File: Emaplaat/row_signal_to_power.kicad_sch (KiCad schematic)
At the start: 11 parts, among them IC2 1EDN7550BXTSA1, IC4 74HC1G04GV-Q100H, IC5 1EDN7550BXTSA1, IC6 74LVC1G66GW,125

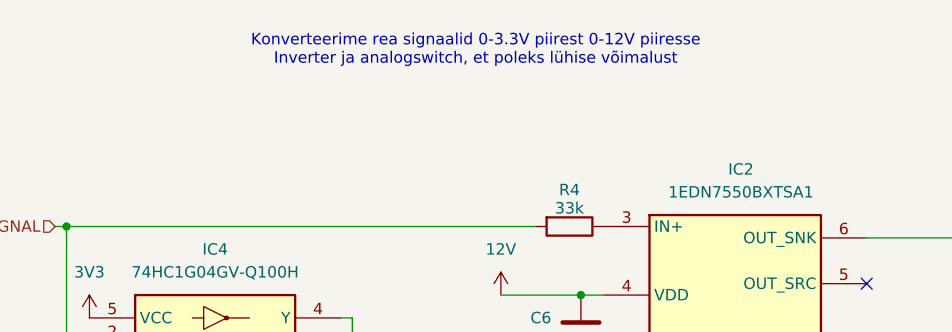
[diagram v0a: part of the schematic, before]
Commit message: 3V3 voolud kontrollitud
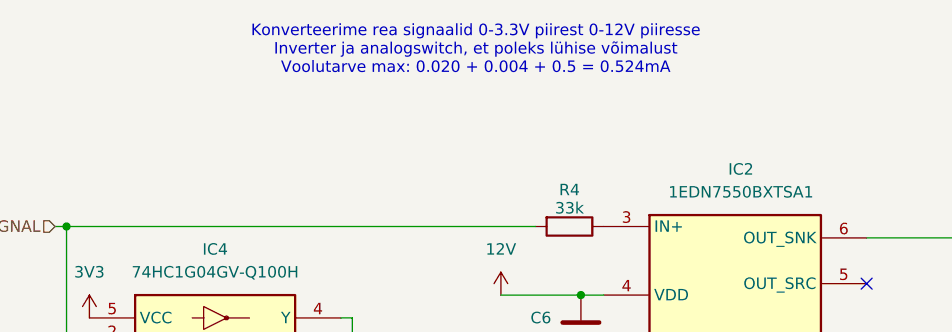
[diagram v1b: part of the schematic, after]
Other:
- note added: "Konverteerime rea signaalid 0-3.3V piirest 0-12V piiresse Inverter ja analogswitch, et poleks lühise võimalust Voolutarve max: 0.020 + 0.004 + 0.5 = 0.524mA"
- note removed: "Konverteerime rea signaalid 0-3.3V piirest 0-12V piiresse Inverter ja analogswitch, et poleks lühise võimalust"
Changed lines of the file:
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@@
 	(generator_version "9.0")
 	(paper "A4")
-	(text "Konverteerime rea signaalid 0-3.3V piirest 0-12V piiresse\nInverter ja analogswitch, et poleks lühise võimalust"
+	(text "Konverteerime rea signaalid 0-3.3V piirest 0-12V piiresse\nInverter ja analogswitch, et poleks lühise võimalust\nVoolutarve max: 0.020 + 0.004 + 0.5 = 0.524mA"
 		(exclude_from_sim no)
 		(at 136.906 38.862 0)

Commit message: jajald
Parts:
- C21: renamed from C6; footprint Capacitor_SMD:C_0201_0603Metric_Pad0.64x0.40mm_HandSolder -> Capacitor_SMD:C_0603_1608Metric_Pad1.08x0.95mm_HandSolder
- C22: renamed from C11; footprint Capacitor_SMD:C_0201_0603Metric_Pad0.64x0.40mm_HandSolder -> Capacitor_SMD:C_0603_1608Metric_Pad1.08x0.95mm_HandSolder
- renumbered IC2 to IC6, IC4 to IC7, IC5 to IC8, IC6 to IC9, R4 to R12, R5 to R13, R8 to R14, R9 to R15, R10 to R16

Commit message: skeem korras
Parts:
- IC6, IC8: footprint SOT95P280X145-6N -> SOT95P280X145-6N:SOT95P280X145-6N
- IC7: footprint SOT95P275X110-5N -> 74HC1G04GV-Q100H:SOT95P275X110-5N
- IC9: footprint SOT65P212X110-5N -> 74LVC1G66GW,125:SOT65P212X110-5N
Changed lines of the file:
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@@
 			)
 		)
-		(property "Footprint" "SOT95P280X145-6N"
+		(property "Footprint" "SOT95P280X145-6N:SOT95P280X145-6N"
 			(at 177.8 186.36 0)
 			(effects
@@
 			)
 		)
-		(property "Footprint" "SOT65P212X110-5N"
+		(property "Footprint" "74LVC1G66GW,125:SOT65P212X110-5N"
 			(at 116.84 188.9 0)
 			(effects
@@
 			)
 		)
-		(property "Footprint" "SOT95P280X145-6N"
+		(property "Footprint" "SOT95P280X145-6N:SOT95P280X145-6N"
 			(at 177.8 154.61 0)
 			(effects
@@
 			)
 		)
-		(property "Footprint" "SOT95P275X110-5N"
+		(property "Footprint" "74HC1G04GV-Q100H:SOT95P275X110-5N"
 			(at 118.11 163.5 0)
 			(effects

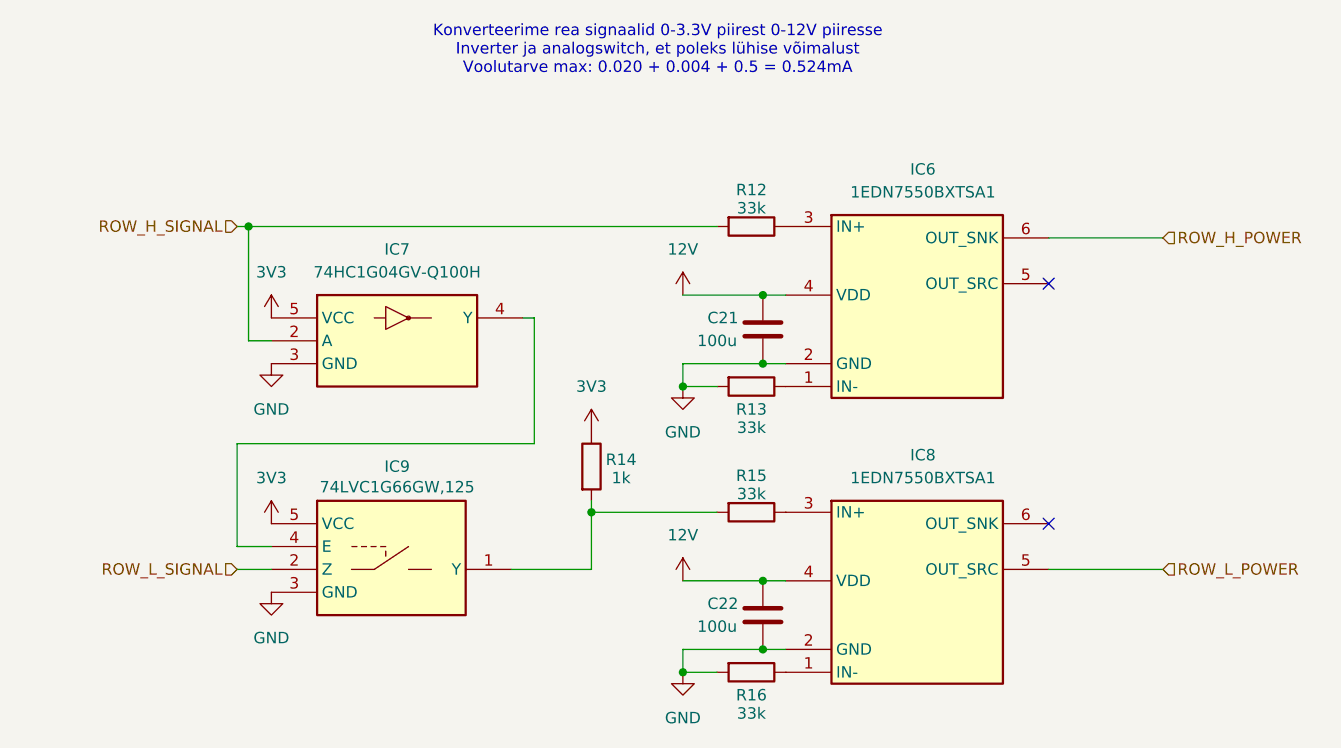
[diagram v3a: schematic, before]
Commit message: Added electrolytic capacitors and 12V rated ESD diode
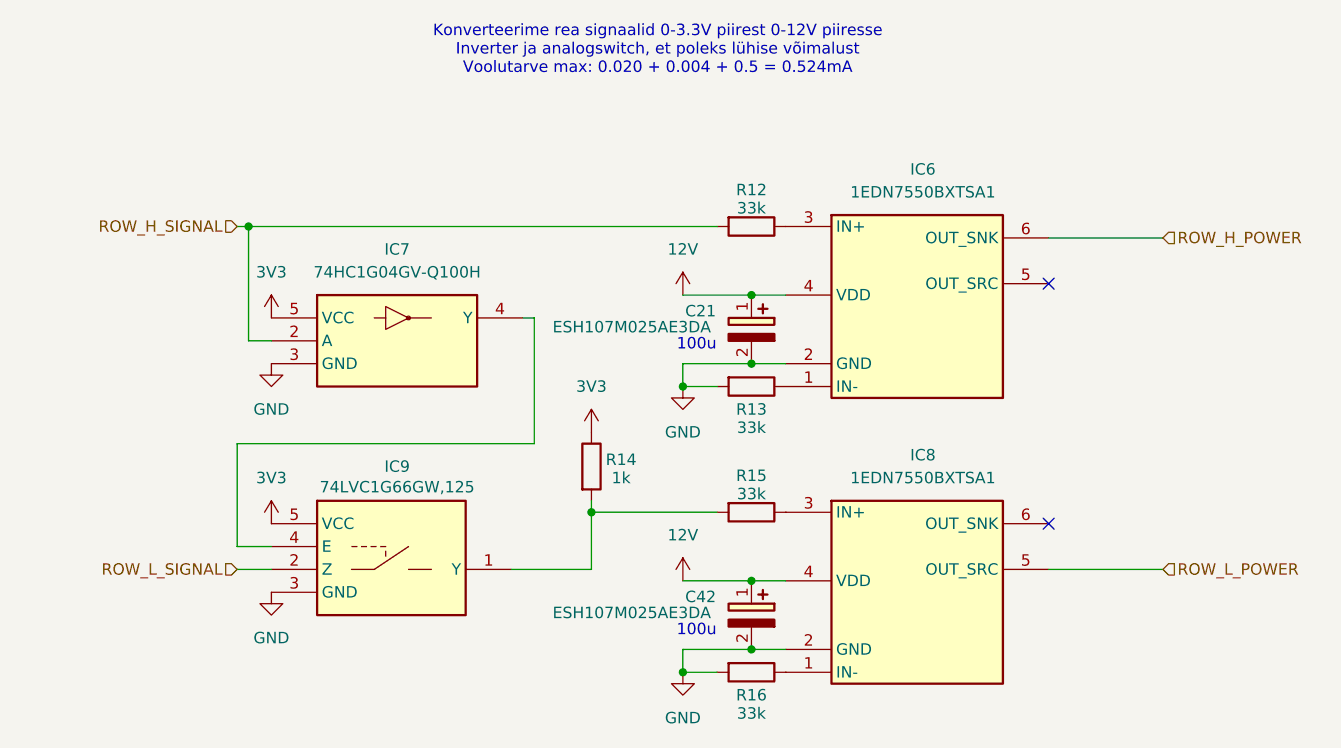
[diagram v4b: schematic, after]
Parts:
- removed C21, C22: 100u, Capacitor_SMD:C_0603_1608Metric_Pad1.08x0.95mm_HandSolder, symbol Device:C
- added C21, C42: ESH107M025AE3DA, CAPPRD250W50D630H1250, symbol ESH107M025AE3DA:ESH107M025AE3DA
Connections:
- net 12V: now also C21.1 (+), C42.1 (+)
- net GND: now also C21.2 (-), C42.2 (-)
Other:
- note added: "100u"

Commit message: v1.5 valmis, juhendajad andsid rohelise tule
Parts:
- added C55, C62: 0.1u, Capacitor_SMD:C_0603_1608Metric_Pad1.08x0.95mm_HandSolder, symbol Device:C
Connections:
- net 3V3: now also C55.1, C62.1
- net GND: now also C55.2, C62.2
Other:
- moved on the sheet: IC7, IC9
